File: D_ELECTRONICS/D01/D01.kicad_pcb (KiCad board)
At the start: 2 copper layers, 58.4 x 48.3 mm, 22 parts, among them J0 Conn_01x01_Male, J1 Conn_01x01_Male, J10 Conn_01x06_Female, J11 Conn_01x02_Female, J2 Conn_01x02_Female, J3 Conn_01x02_Female, J4 RJ45, J5 RJ45, J6 USB_A, J7 Conn_01x02_Female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

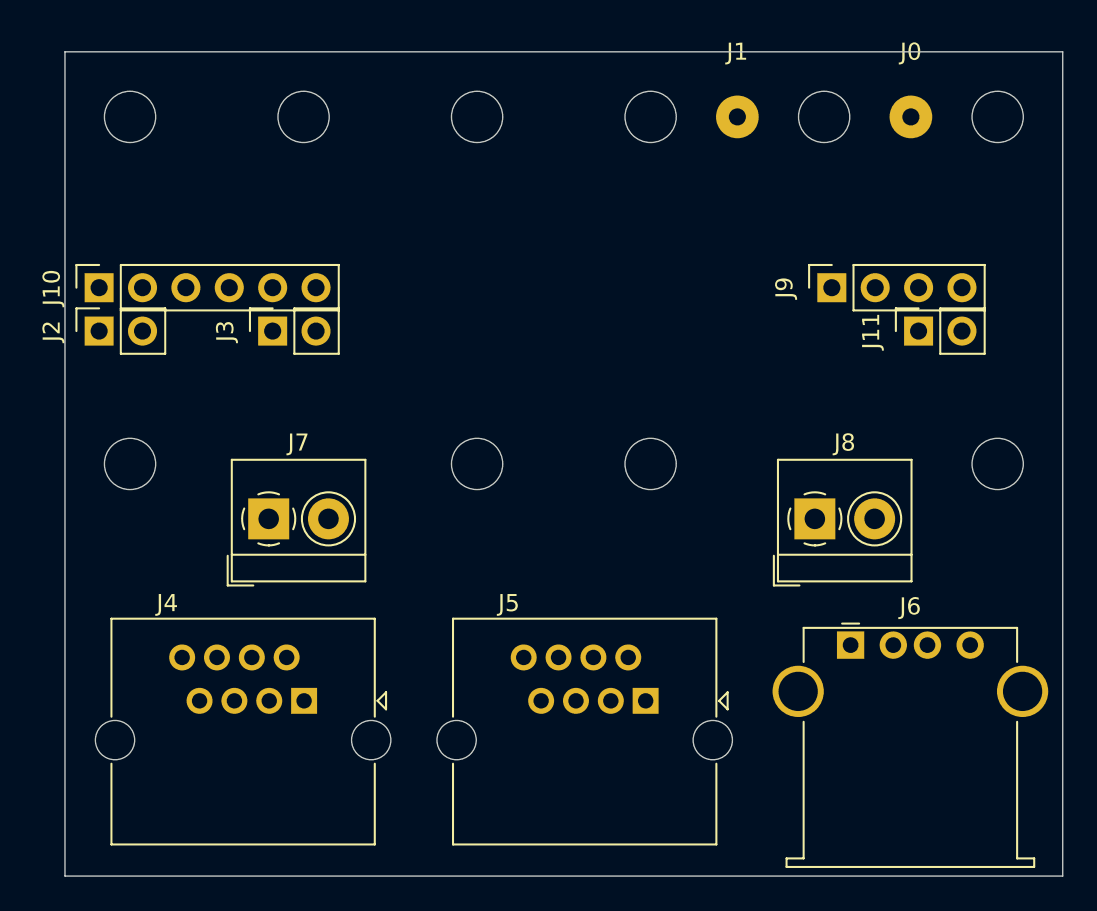
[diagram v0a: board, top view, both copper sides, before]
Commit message: D01 all traces routed
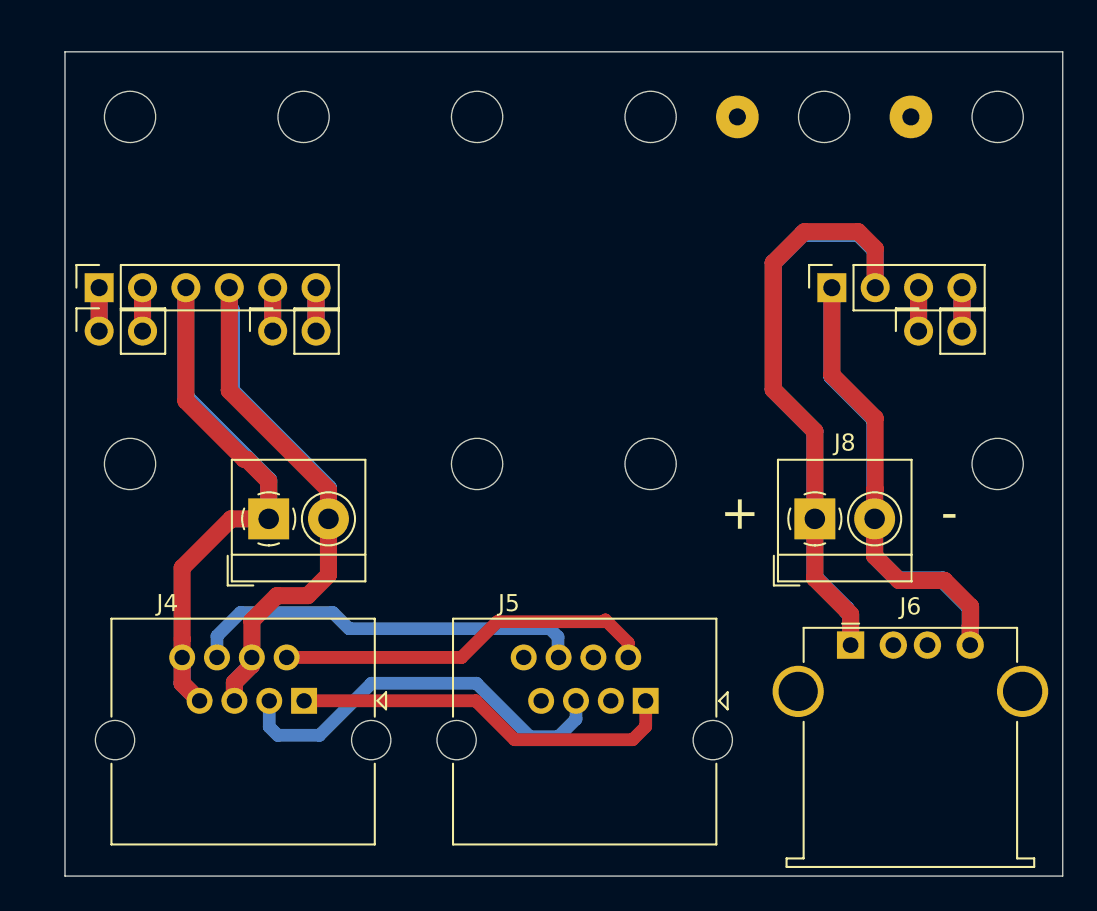
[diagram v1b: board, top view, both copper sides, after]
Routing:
- net Net-(J6-Pad1): track 0.00 -> 67.3 mm
- net Net-(J6-Pad4): track 0.00 -> 51.7 mm
- net Net-(J10-Pad4): track 0.00 -> 48.8 mm
- net Net-(J10-Pad3): track 0.00 -> 48.6 mm
- net Net-(J4-Pad3): track 0.00 -> 23.7 mm
- net Net-(J4-Pad6): track 0.00 -> 23.6 mm
- net Net-(J4-Pad1): track 0.00 -> 22.8 mm
- net Net-(J4-Pad2): track 0.00 -> 22.3 mm
- net Net-(J11-Pad2): track 0.00 -> 5.08 mm
- net Net-(J11-Pad1): track 0.00 -> 5.08 mm
- net Net-(J10-Pad6): track 0.00 -> 5.08 mm
- net Net-(J10-Pad5): track 0.00 -> 5.08 mm
- net Net-(J10-Pad2): track 0.00 -> 5.08 mm
- net Net-(J10-Pad1): track 0.00 -> 5.08 mm
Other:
- net class Default: trace_width 0.25 -> 1
- board text added: "+"
- board text added: "-"

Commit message: D01 single gerber
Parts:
- added REF**: OSHW-Symbol_6.7x6mm_Copper, Symbol:OSHW-Symbol_6.7x6mm_Copper, B.Cu at (49.0, 39.2)
- added REF**: OSHW-Symbol_6.7x6mm_Copper, Symbol:OSHW-Symbol_6.7x6mm_Copper, F.Cu at (49.1, 38.6)
- added REF**: OSHW-Symbol_6.7x6mm_SilkScreen, Symbol:OSHW-Symbol_6.7x6mm_SilkScreen, B.Cu at (29.0, 28.5)
- added REF**: OSHW-Symbol_6.7x6mm_SilkScreen, Symbol:OSHW-Symbol_6.7x6mm_SilkScreen, F.Cu at (50.0, 63.0)
- moved J1 29.6 mm to (74.6, 49.2)
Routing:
- added copper zone on B.Cu, net Net-(J0-Pad1)
- added copper zone on F.Cu, net Net-(J0-Pad1)
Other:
- board text added: "D01_ELECTRONIC"
